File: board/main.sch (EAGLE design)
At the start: 53 parts, among them IC2 L6387EDIP8, IC3 L6387EDIP8, IC4 L6387EDIP8, J3 FUSE, Q1 MOSFET-NCHANNELTO-220-FLAT, Q2 MOSFET-NCHANNELTO-220-FLAT, Q3 MOSFET-NCHANNELTO-220-FLAT, Q4 MOSFET-NCHANNELTO-220-FLAT, Q5 MOSFET-NCHANNELTO-220-FLAT, Q6 MOSFET-NCHANNELTO-220-FLAT

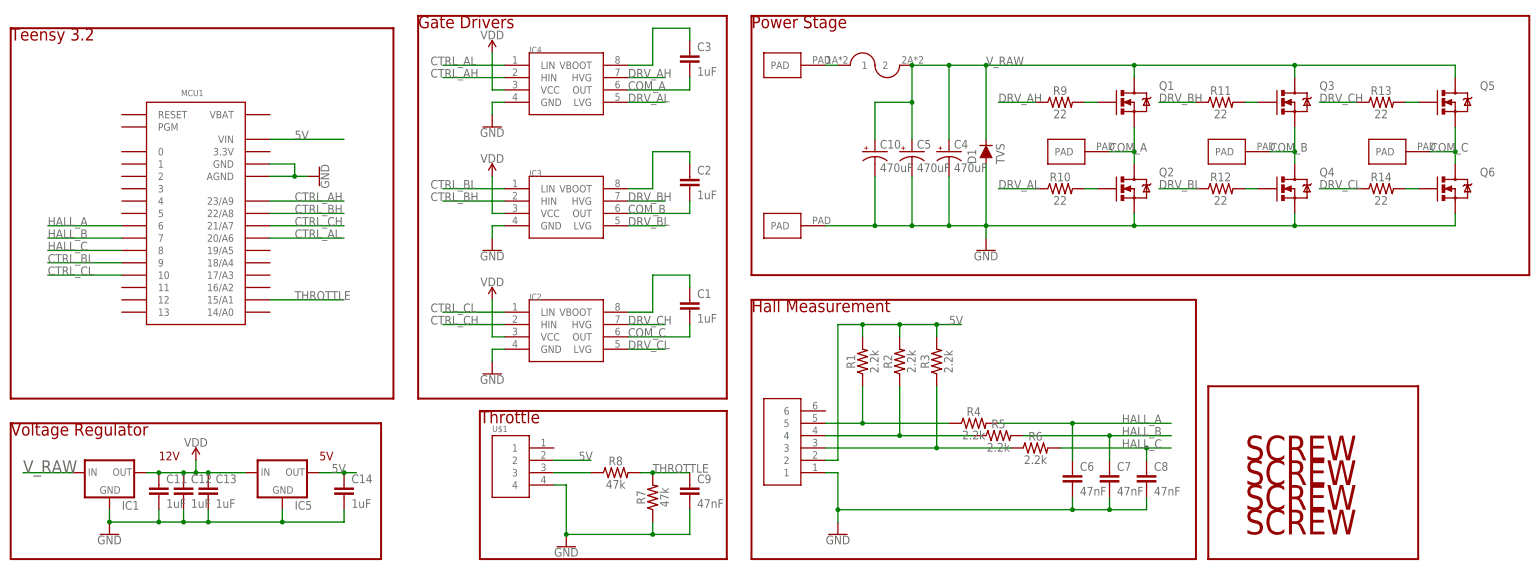
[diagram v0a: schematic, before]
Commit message: Added connectors to BOM
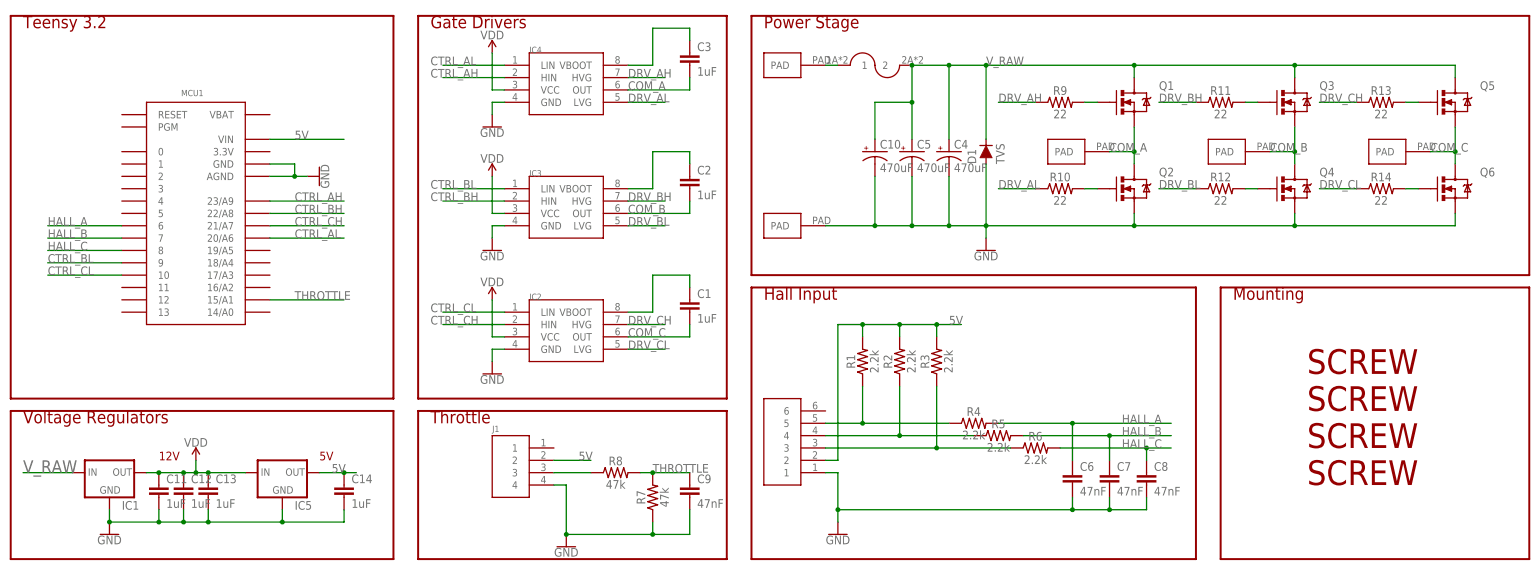
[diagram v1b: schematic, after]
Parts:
- renumbered U$1 to J1, U$2 to J2
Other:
- note added: "Hall Input"
- note added: "Mounting"
- note added: "Voltage Regulators"
- note removed: "Hall Measurement"
- note removed: "Voltage Regulator"
